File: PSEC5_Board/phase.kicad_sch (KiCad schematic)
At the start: 10 parts, among them U1 MCP1700T-1802E_TT, U5 MC100LVEL, U6 OPA607QDBVRQ1, U7 AD4008BCPZ-RL7, Y1 ASE2-40.000MHZ-ET

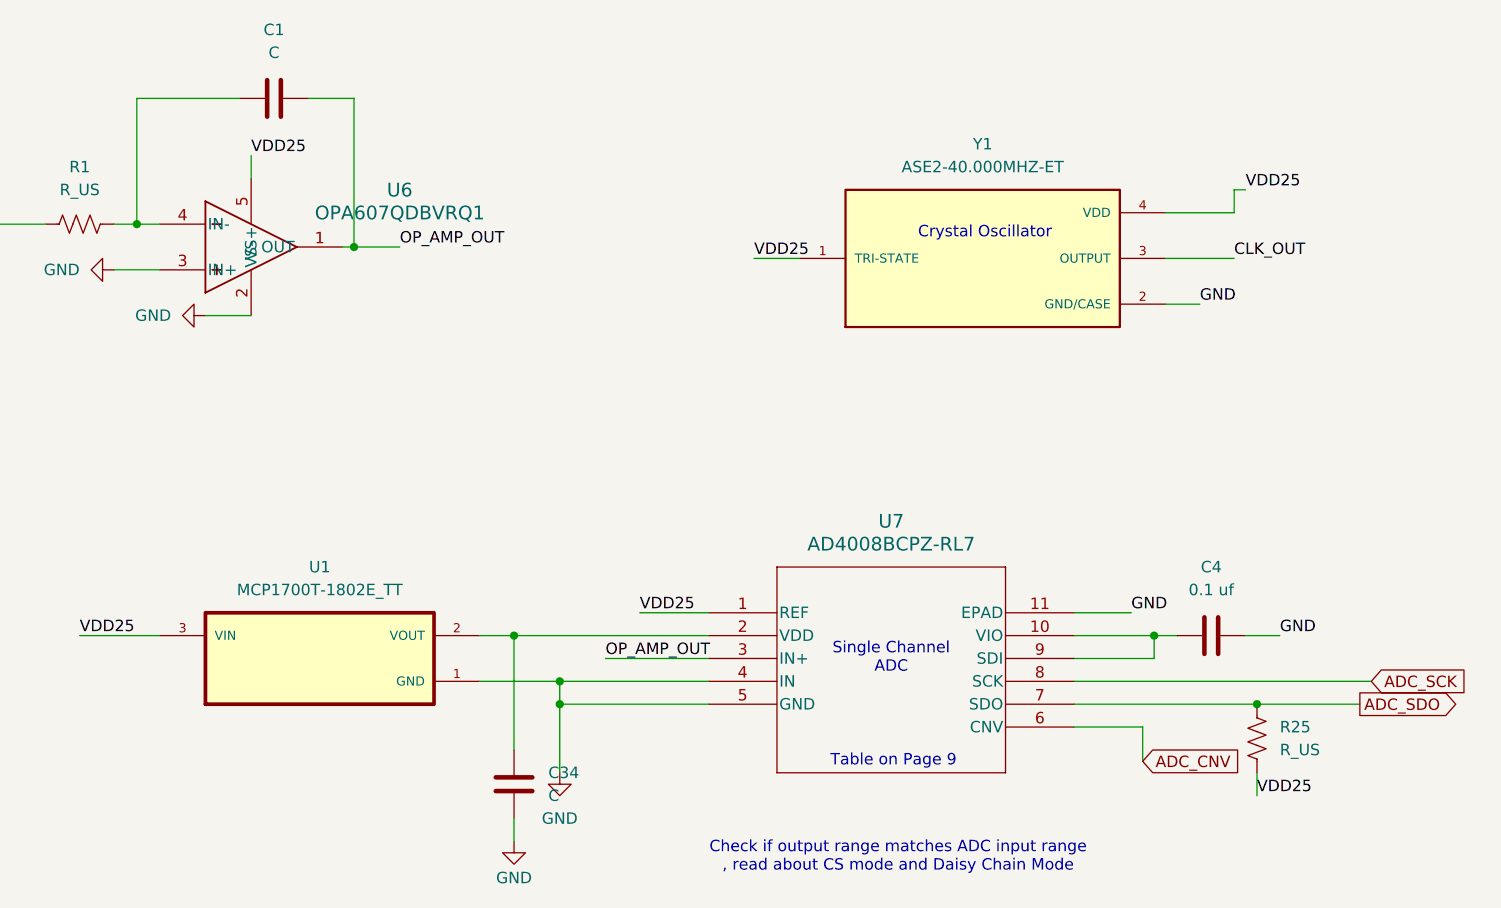
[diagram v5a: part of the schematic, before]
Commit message: DUT Layout Overhaul
Footprints need to be replaced.
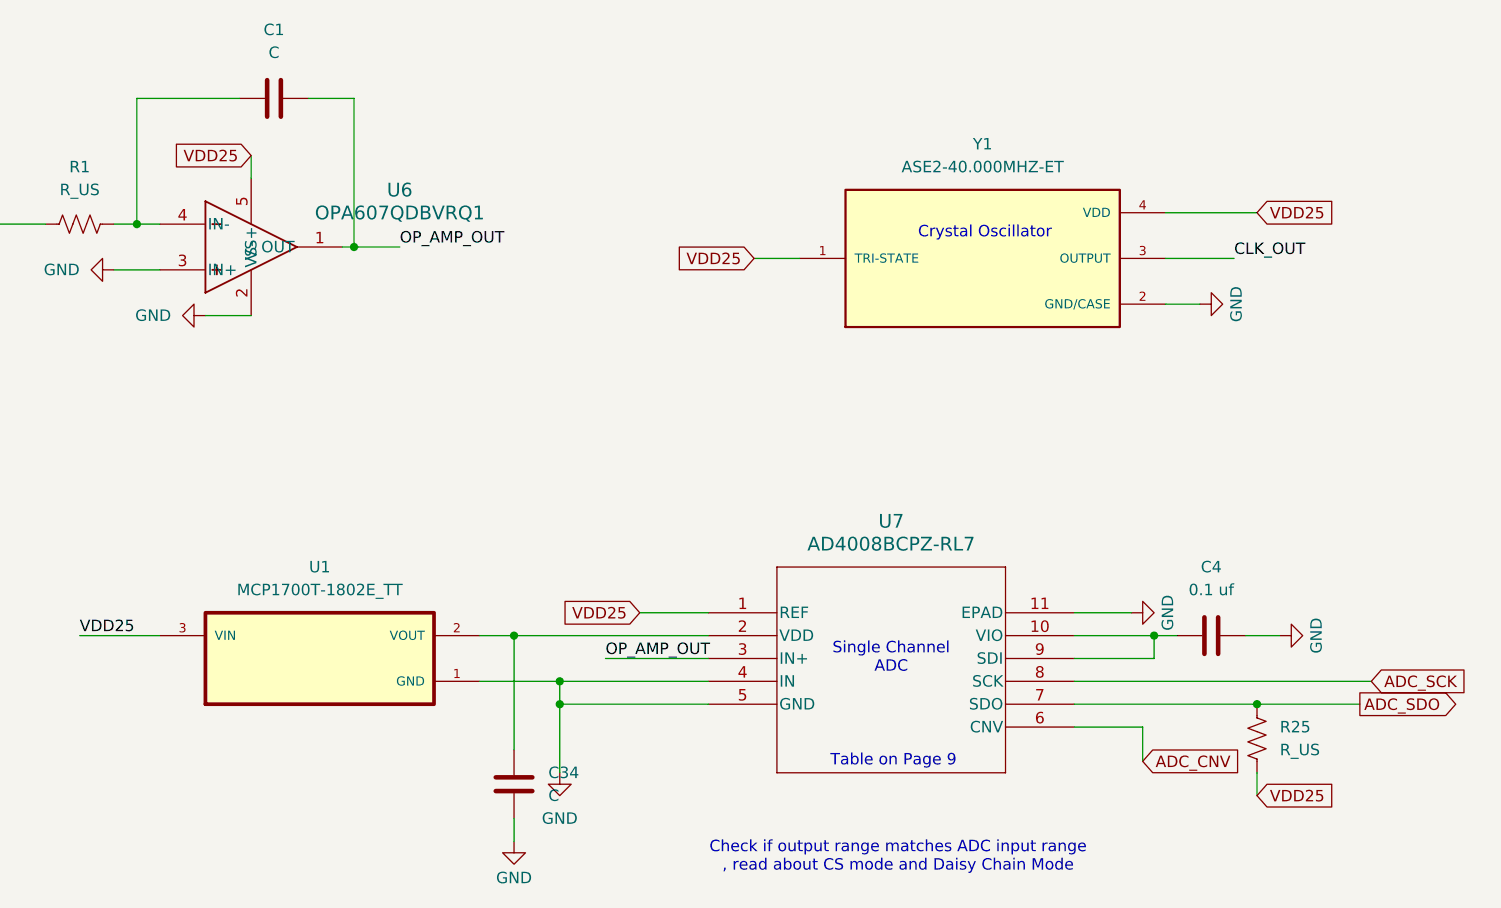
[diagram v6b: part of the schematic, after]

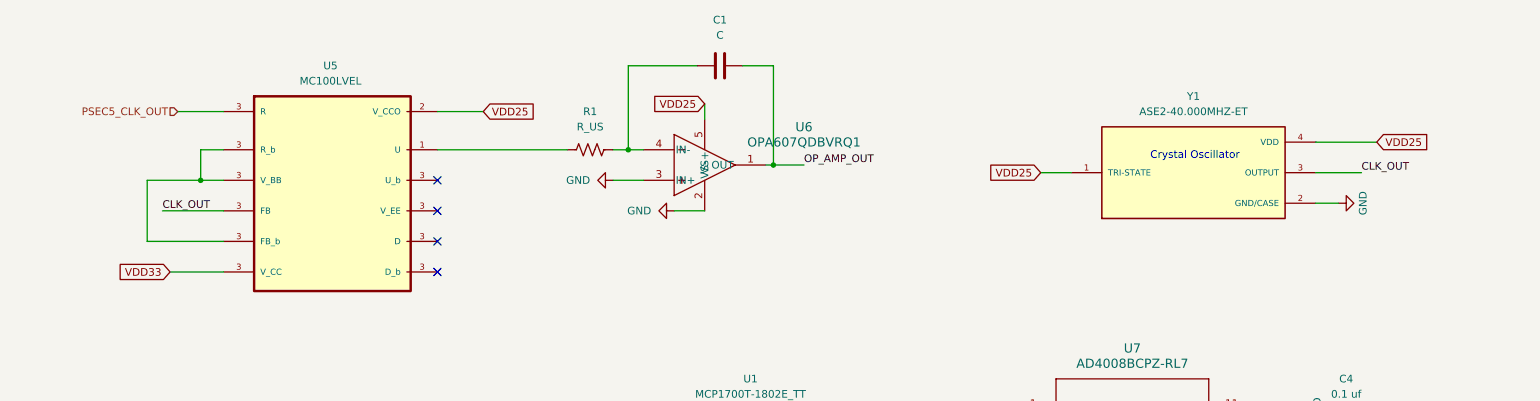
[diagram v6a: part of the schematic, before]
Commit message: DUT push - All nets
All nets are connected, Power and ground planes not registering.

ERC not completed.
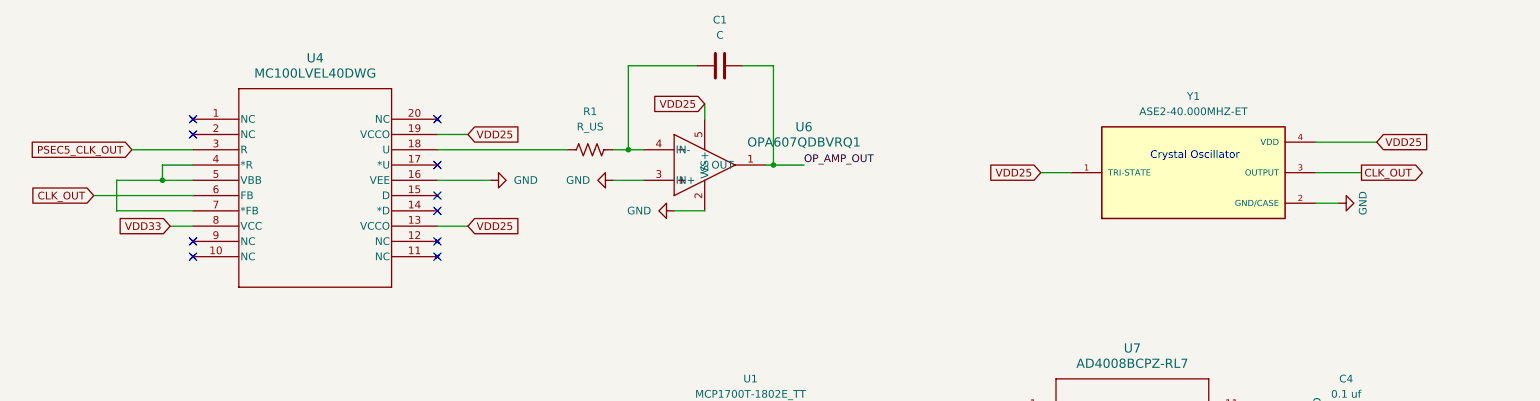
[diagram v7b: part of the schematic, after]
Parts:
- removed U5: MC100LVEL, MCP1700T_1802E_TT:SOT95P237X112-3N, symbol MCP1700T-1802E_TT:MCP1700T-1802E_TT
- added U4: MC100LVEL40DWG, MC100LVEL40DWG:SOP65P640X120-20N, symbol MC100LVEL40DWG_B:MC100LVEL40DWG
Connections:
- net CLK_OUT: now also U4.6 (FB)
- net GND: now also U4.16 (VEE)
- net PSEC5_CLK_OUT: now also U4.3 (R)
- net VDD25: now also U4.13 (VCCO), U4.19 (VCCO)
- net VDD33: now also U4.8 (VCC)
- net at R1.2: now also U4.18 (U)
- new net: U4.4 (*R), U4.5 (VBB), U4.7 (*FB)
- no-connect marks 4 -> 10

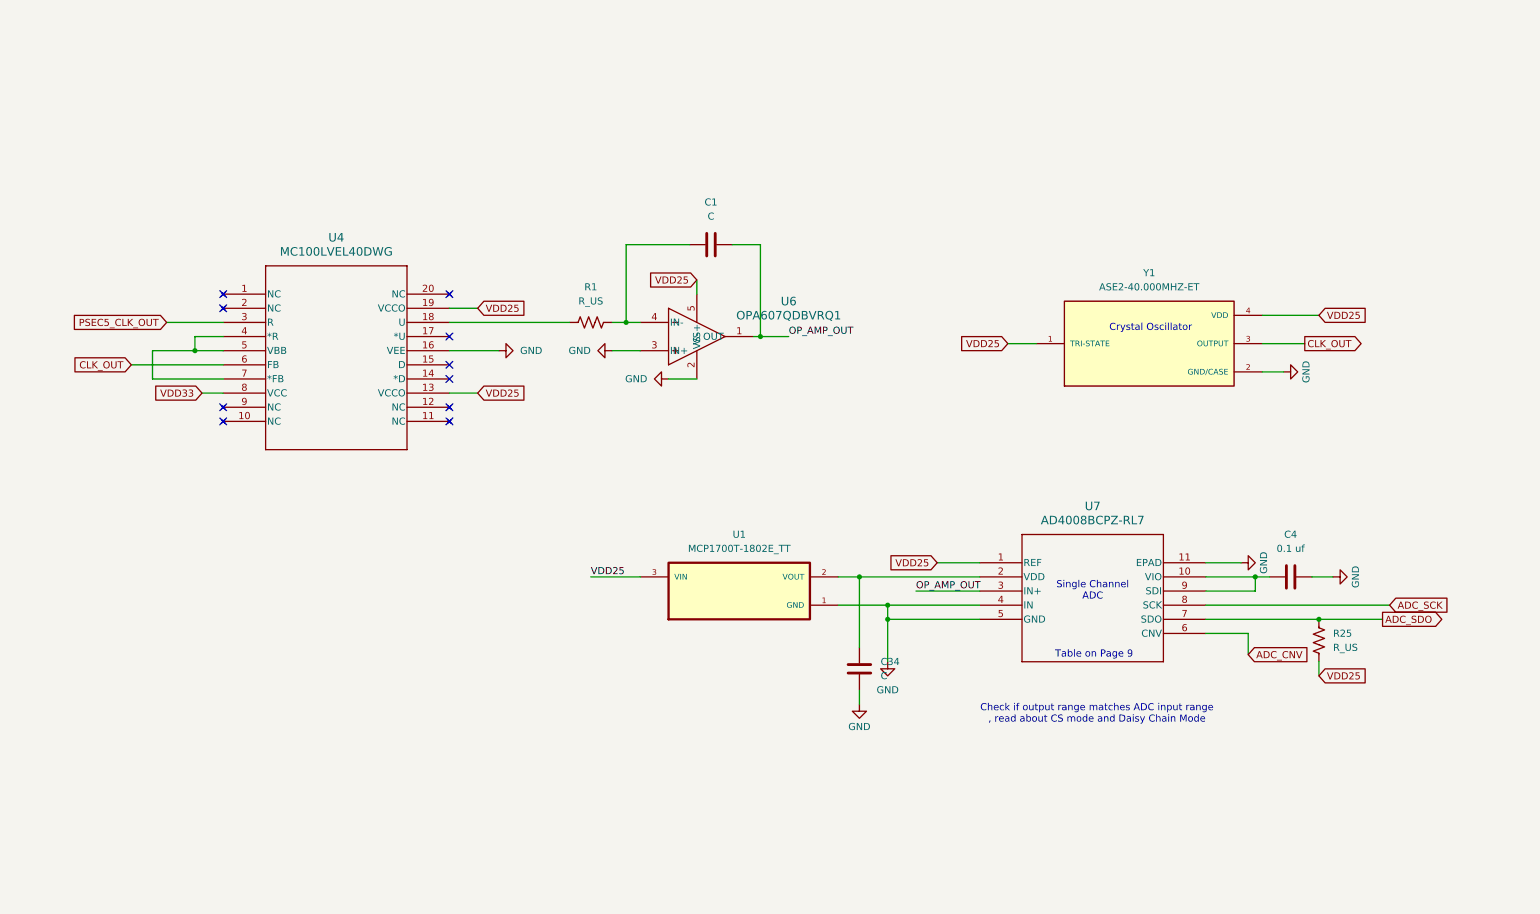
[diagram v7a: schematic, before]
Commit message: DUT v4 Push
Addressed the issues discussed in last week's meeting, cleared ERC errors, still any warnings with Solder Mask.
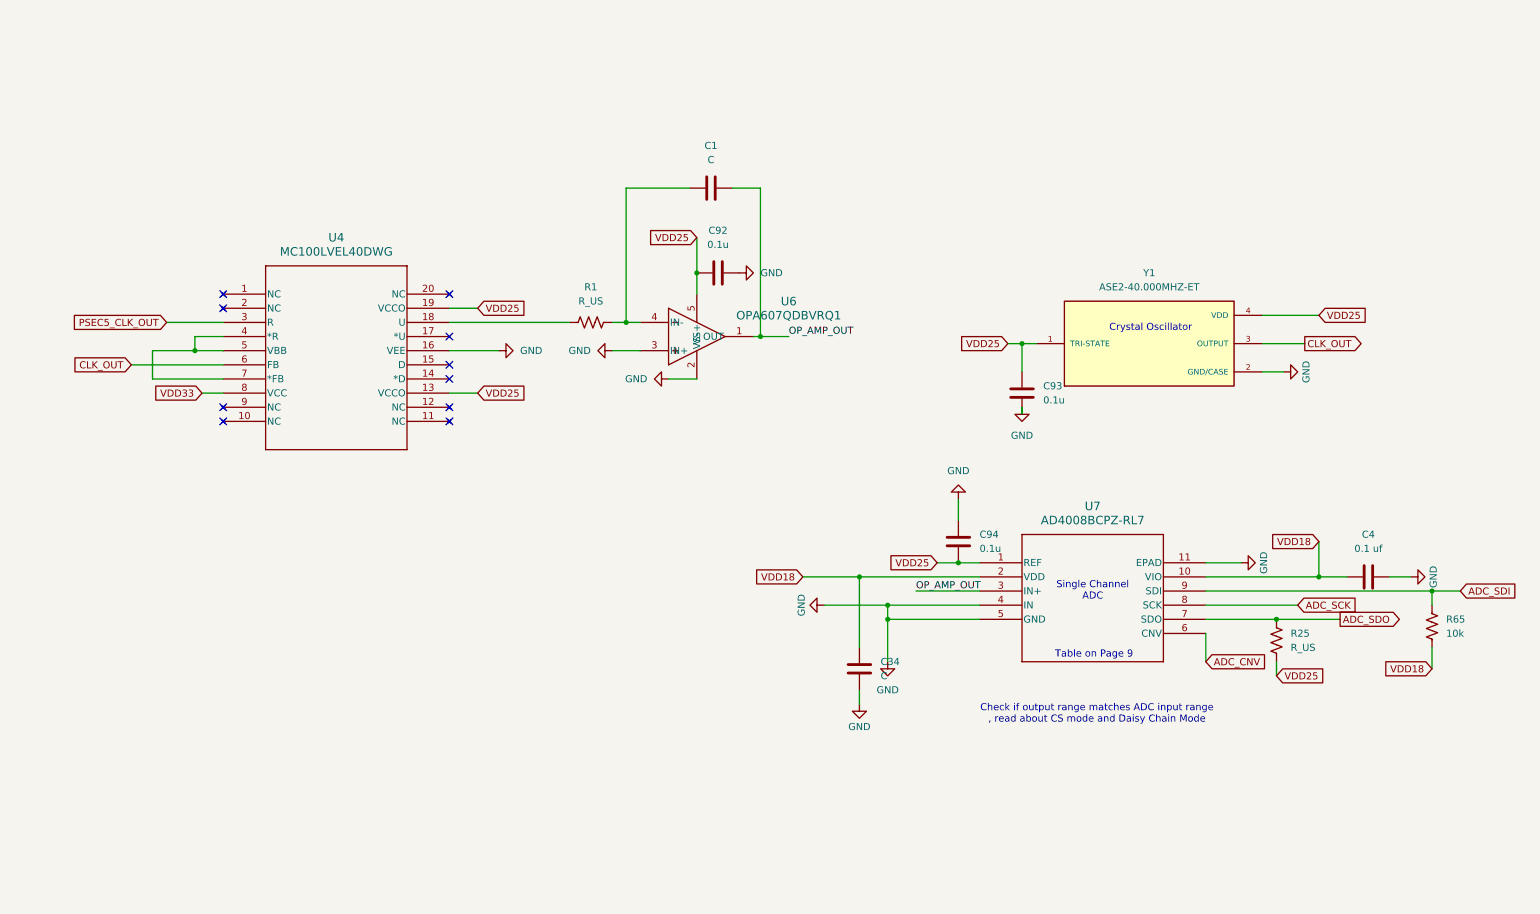
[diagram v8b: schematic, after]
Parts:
- removed U1: MCP1700T-1802E_TT, MCP1700T_1802E_TT:SOT95P237X112-3N, symbol MCP1700T-1802E_TT:MCP1700T-1802E_TT
- added C92, C93, C94: 0.1u, Capacitor_SMD:C_0603_1608Metric, symbol Device:C
- added R65: 10k, Resistor_SMD:R_0603_1608Metric, symbol Device:R_US
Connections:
- net GND: now also C92.1, C93.1, C94.2
- net VDD25: now also C92.2, C93.2, C94.1
- net VDD18: now reaches C4.2, U7.10 (VIO)
- net VDD18: now also C34.1, U7.2 (VDD), R65.1; no longer U7.9 (SDI)
- new net ADC_SDI: R65.2, U7.9 (SDI)
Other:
- moved on the sheet: C1, C4, R25
